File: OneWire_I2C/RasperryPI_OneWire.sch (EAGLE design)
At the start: 21 parts, among them U1 P82B715D, U2 DS2482-800

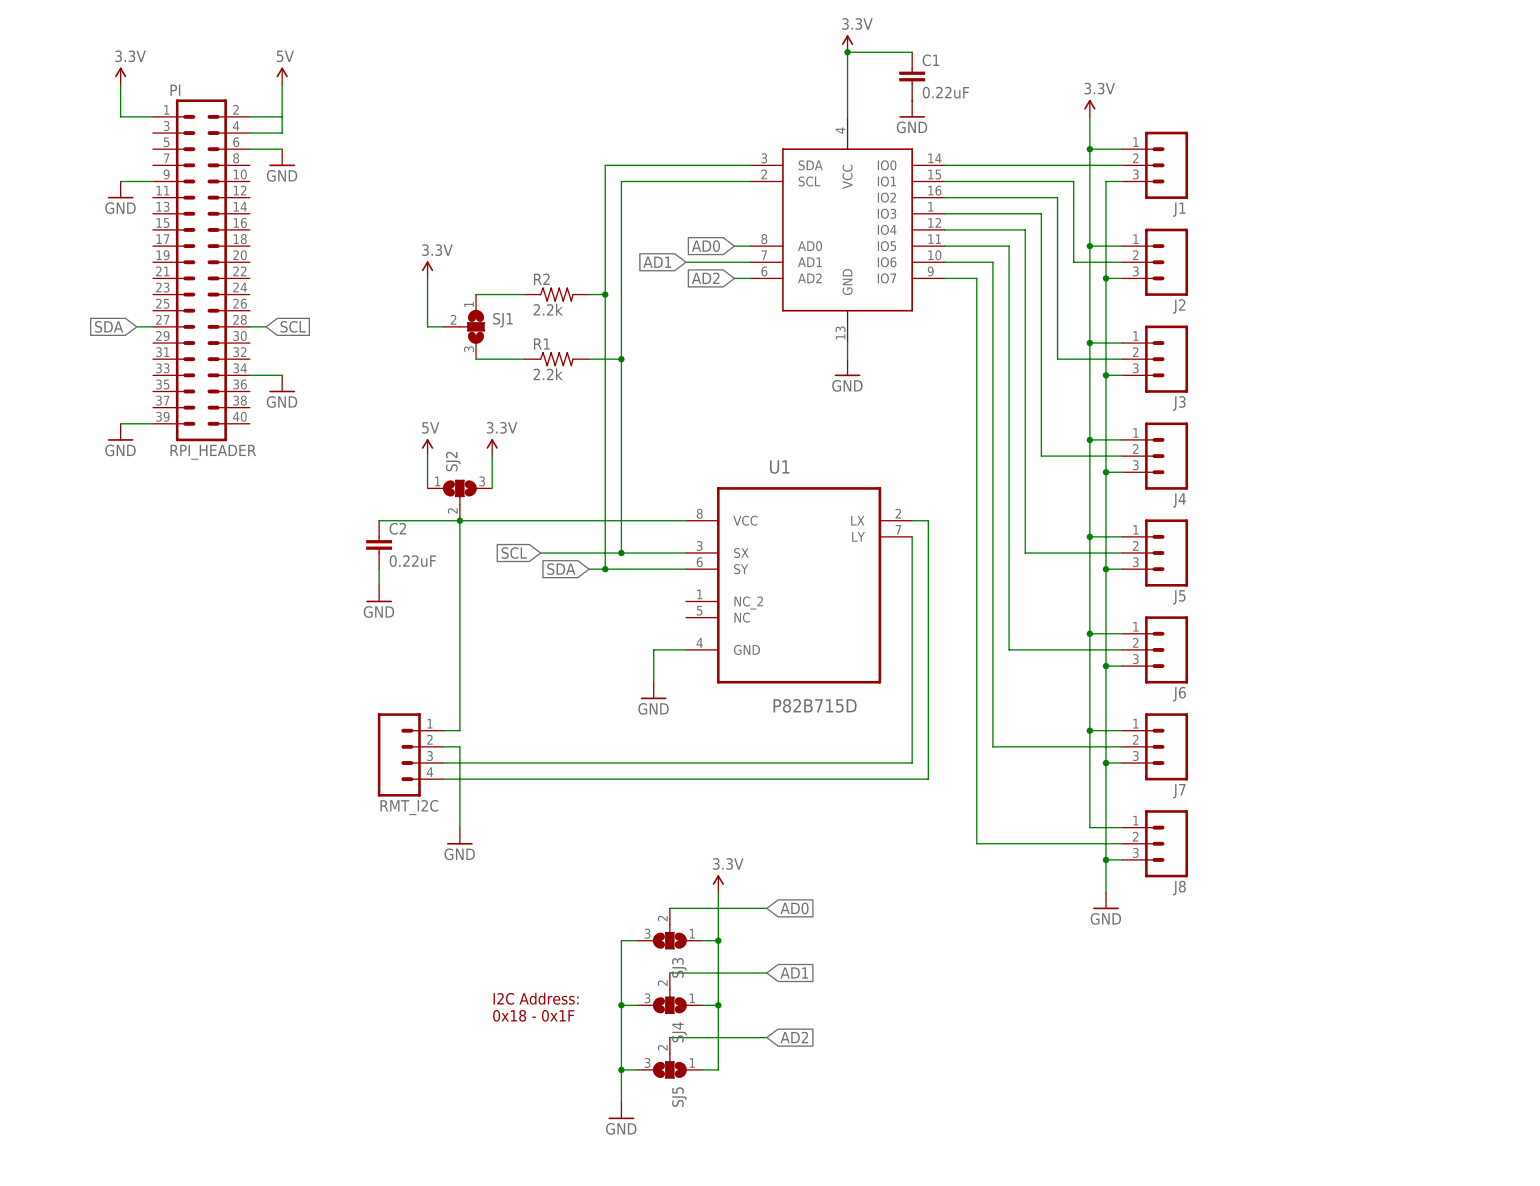
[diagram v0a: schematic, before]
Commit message: Added Raspberry pi board, updated I2C extender pullup resistors to other boards
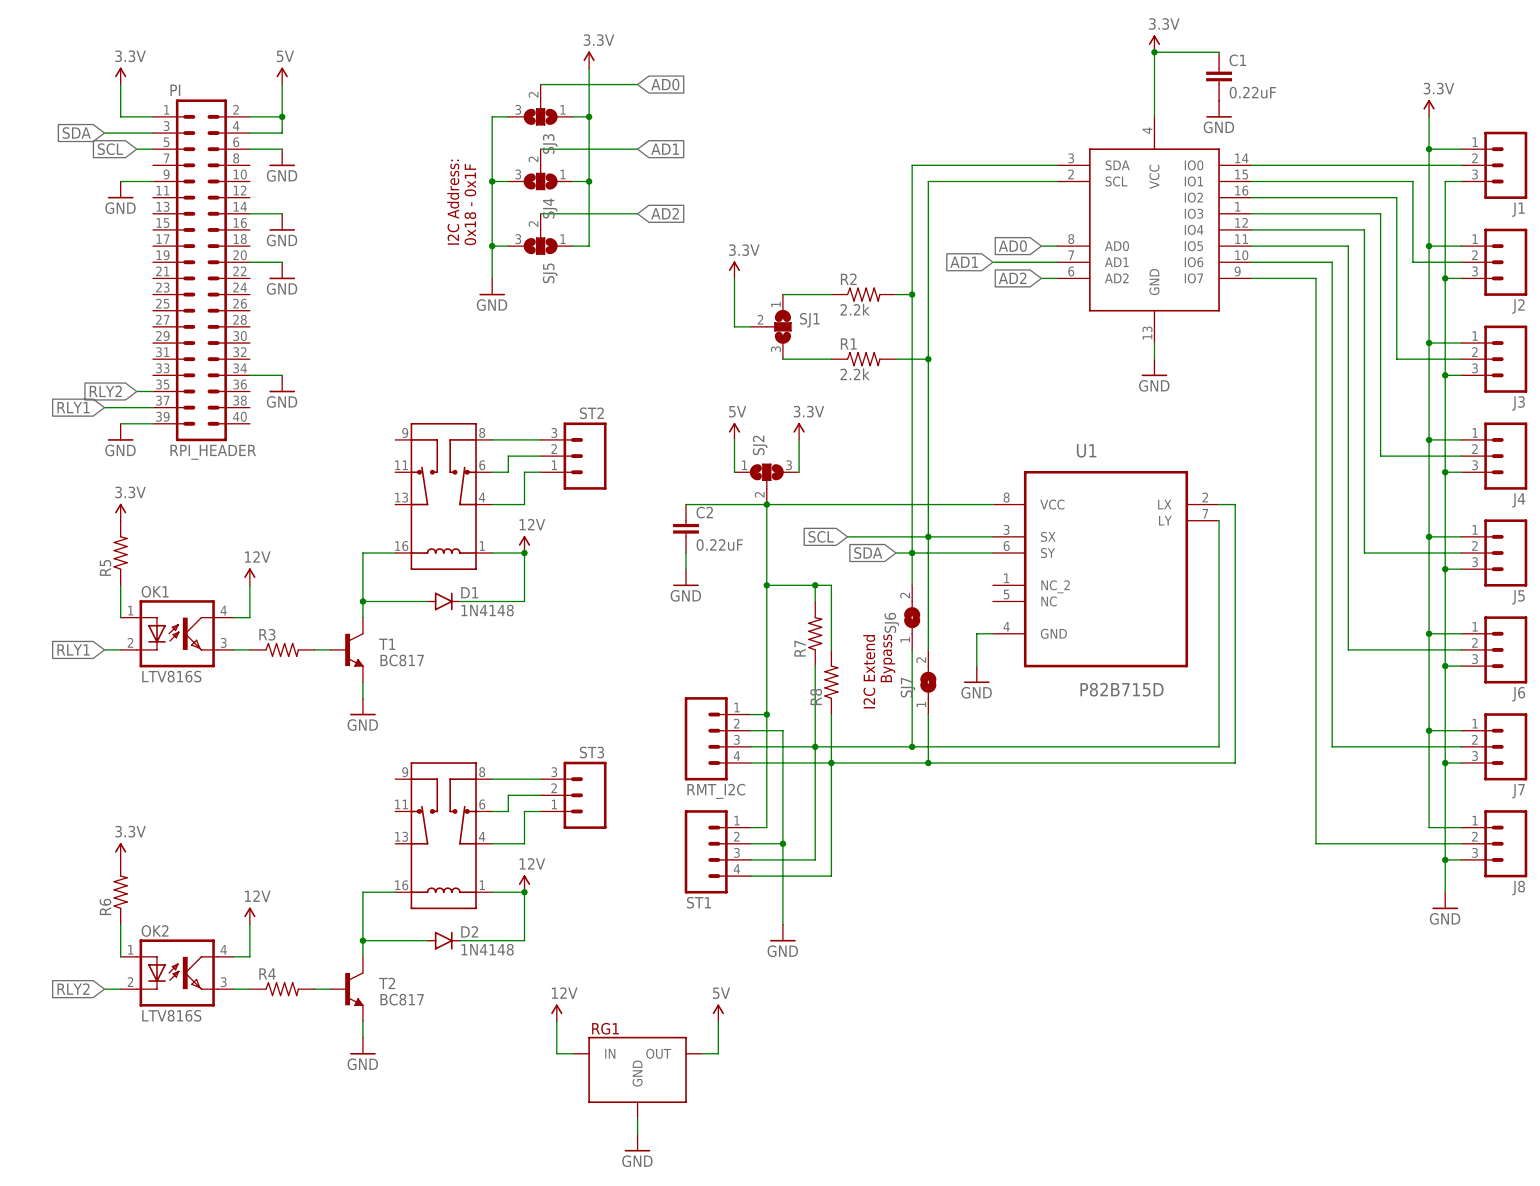
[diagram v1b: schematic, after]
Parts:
- added D1, D2: 1N4148, SparkFun-DiscreteSemi:DIODE1N4148
- added OK1, OK2: LTV816S, optocoupler:LTV816S
- added R3, R4: (no value), SparkFun-Resistors:RESISTOR0603
- added R5, R6, R7, R8: (no value), SparkFun-Resistors:RESISTOR0805-RES
- added RG1: (no value), Puffin:MURATA_REG
- added RLY1, RLY2: HK19F_5V_DPDT_RELAY, Puffin:HK19F_5V_DPDT_RELAY
- added SJ6, SJ7: (no value), jumper:SJ
- added ST1: (no value), Puffin:SCREWTERM_4
- added ST2, ST3: (no value), Puffin:SCREWTERM_3
- added T1, T2: BC817, Puffin:BC817
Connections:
- new net 12V: D1.C, D2.C, OK1.COL, OK2.COL, RG1.IN, RLY1.L1, RLY2.L1
- new net N$12: R4.2, T2.B
- new net N$13: D2.A, RLY2.L2, T2.C
- new net N$14: D1.A, RLY1.L2, T1.C
- new net N$15: R3.2, T1.B
- new net N$16: OK1.EMIT, R3.1
- new net N$17: RLY2.C1, ST3.1
- new net N$18: RLY2.NC1, ST3.2
- new net N$19: RLY2.NO1, ST3.3
- new net N$20: RLY1.C1, ST2.1
- new net N$21: RLY1.NC1, ST2.2
- new net N$22: RLY1.NO1, ST2.3
- new net N$23: OK2.A, R6.1
- new net N$24: OK1.A, R5.1
- new net RLY1: OK1.C, PI.37
- new net RLY2: OK2.C, PI.35
- new net VSEL: C2.1, R7.2, R8.2, RMT_I2C.1, SJ2.2, ST1.1, U1.VCC
- net 3.3V: now also R5.2, R6.2
- net 5V: now also RG1.OUT
- net GND: now also PI.14, PI.20, RG1.GND, ST1.2, T1.E, T2.E
- net LCL: now also R8.1, SJ7.1, ST1.4
- net LDA: now also R7.1, SJ6.1, ST1.3
- net N$11: now also OK2.EMIT, R4.1; no longer C2.1, RMT_I2C.1, SJ2.2, U1.VCC
- net SCL: now also PI.5, SJ7.2; no longer PI.28
- net SDA: now also PI.3, SJ6.2; no longer PI.27
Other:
- note added: "I2C Extend Bypass"
- moved on the sheet: C1, C2, J1, J2, J3, J4, J5, J6, J7, J8, R1, R2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

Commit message: Finished RPI 1Wire board
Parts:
- removed RMT_I2C: (no value), SparkFun-Connectors:M04PTH
- removed SJ1: (no value), jumper:SJ2W
- removed ST1: (no value), Puffin:SCREWTERM_4
- added J10, J11, J9: MOLEX_MINILITE_TRAP_2, Puffin:MOLEX_MINILITE_TRAP_2
- added R10, R9: (no value), Puffin:POT_3MM
- R1, R2: value 2.2k -> (none); device SparkFun-Resistors:2.2KOHM-1/10W-1%(0603) -> SparkFun-Resistors:RESISTOR0805-RES
- R3, R4: device SparkFun-Resistors:RESISTOR0603 -> SparkFun-Resistors:RESISTOR0805-RES
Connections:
- removed net N$8: R2.1, SJ1.1
- removed net N$9: R1.1, SJ1.3
- new net N$25: R10.2, R7.2
- new net N$26: R8.2, R9.2
- net 12V: now also J11.1, J9.1
- net 3.3V: now also J1.2, J2.2, J3.2, J4.2, J5.2, J6.2, J7.2, J8.2, R1.2, R2.2; no longer J1.1, J2.1, J3.1, J4.1, J5.1, J6.1, J7.1, J8.1, R5.2, R6.2, SJ1.2
- net GND: now also J10.2, J11.2, R5.1, R6.1; no longer RMT_I2C.2, ST1.2
- net LCL: now also J10.1; no longer RMT_I2C.4, ST1.4
- net LDA: now also J9.2; no longer RMT_I2C.3, ST1.3
- net N$1: now also J1.1; no longer J1.2
- net N$10: now also J8.1; no longer J8.2
- net N$17: now also RLY2.C2
- net N$18: now also RLY2.NC2
- net N$19: now also RLY2.NO2
- net N$2: now also J2.1; no longer J2.2
- net N$20: now also RLY1.C2
- net N$21: now also RLY1.NC2
- net N$22: now also RLY1.NO2
- net N$23: now also OK1.C, R5.2; no longer OK2.A, R6.1
- net N$24: now also OK2.C, R6.2; no longer OK1.A, R5.1
- net N$3: now also J3.1; no longer J3.2
- net N$4: now also J4.1; no longer J4.2
- net N$5: now also J5.1; no longer J5.2
- net N$6: now also J6.1; no longer J6.2
- net N$7: now also J7.1; no longer J7.2
- net RLY1: now also OK1.A; no longer OK1.C
- net RLY2: now also OK2.A; no longer OK2.C
- net SCL: now also R2.1; no longer R1.2
- net SDA: now also R1.1; no longer R2.2
- net VSEL: now also R10.1, R9.1; no longer R7.2, R8.2, RMT_I2C.1, ST1.1
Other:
- moved on the sheet: C2, D1, D2, OK1, OK2, R1, R2, R3, R4, R5, R6, R7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

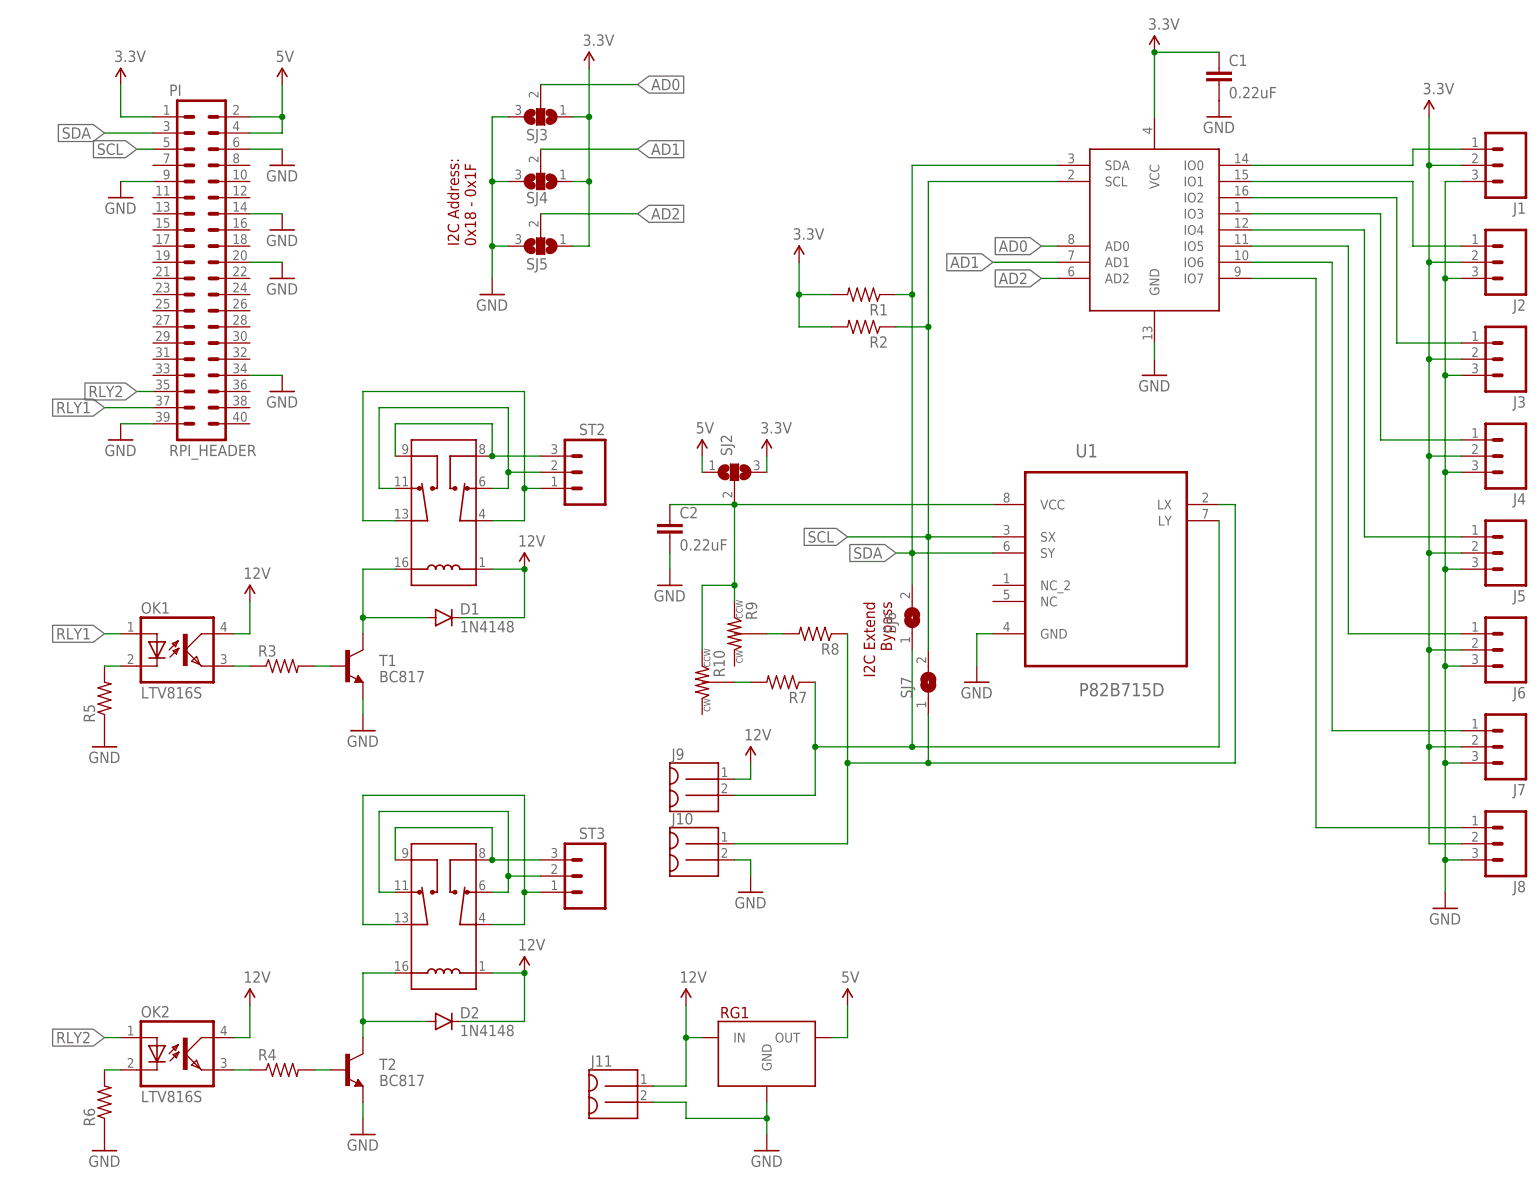
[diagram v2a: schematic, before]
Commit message: Standardized i2c connections, fixed 1Wire connections, lots of cleanup
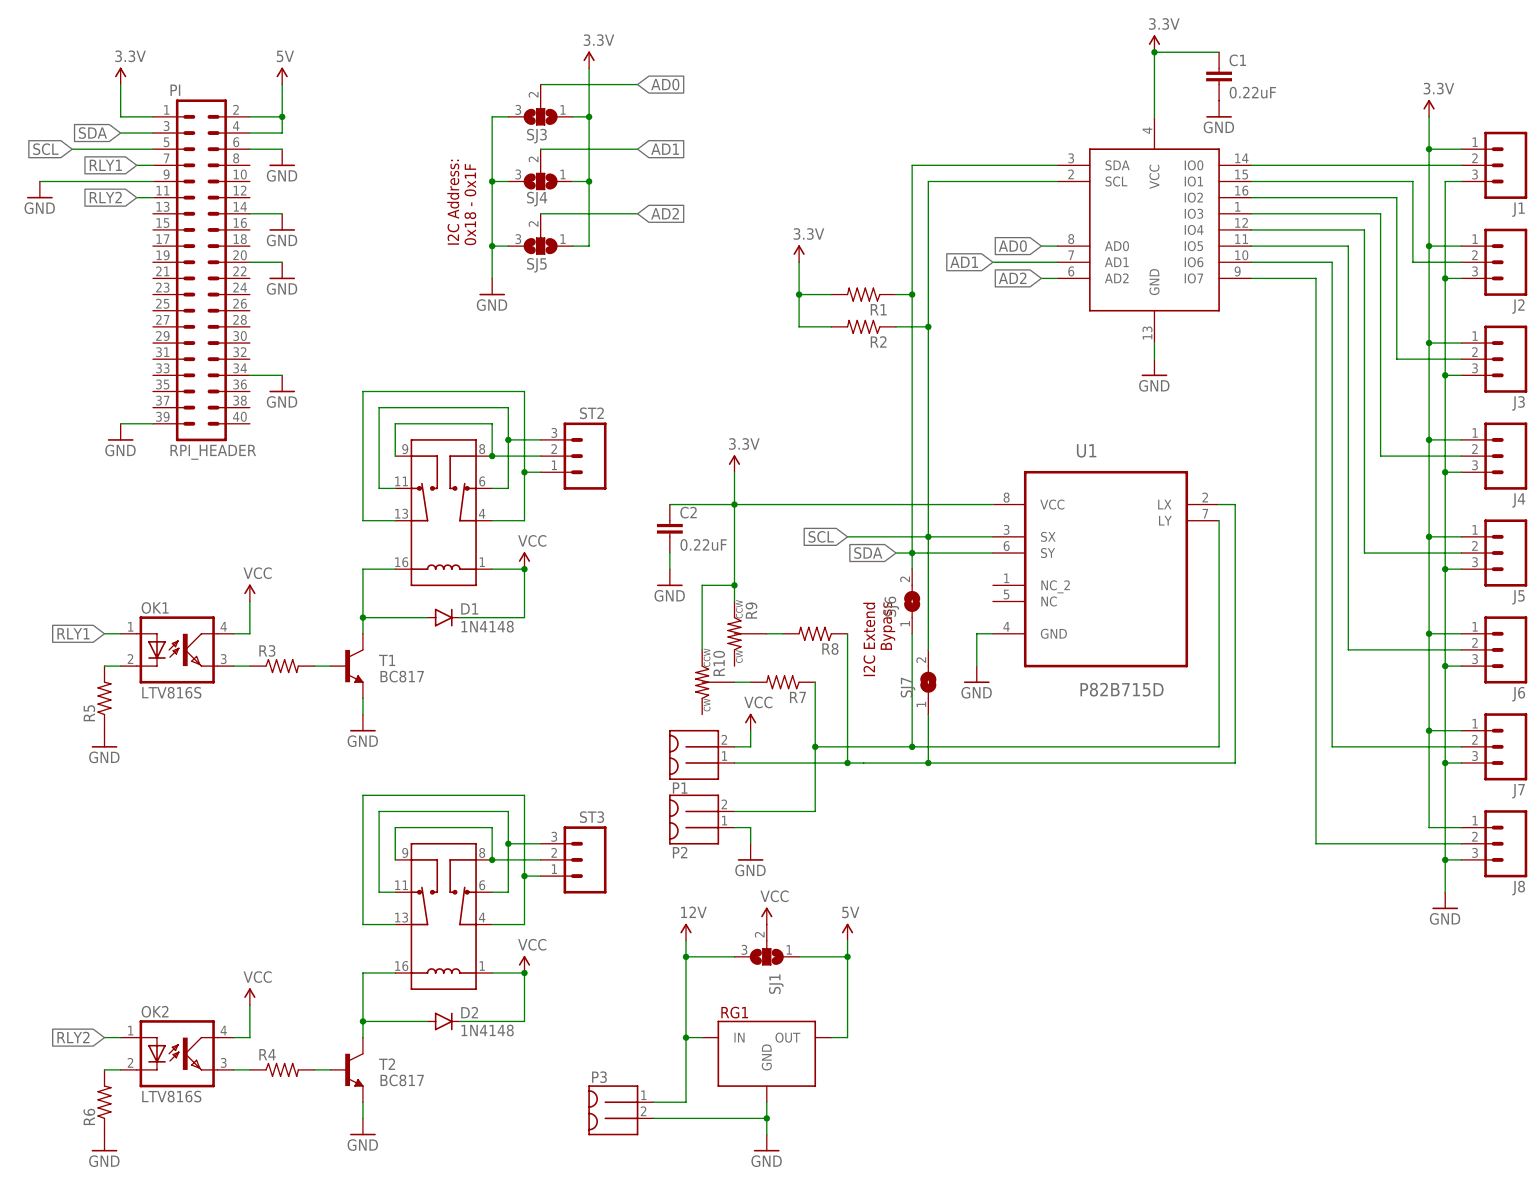
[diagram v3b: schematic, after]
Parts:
- removed J10, J11, J9: MOLEX_MINILITE_TRAP_2, Puffin:MOLEX_MINILITE_TRAP_2
- removed SJ2: (no value), jumper:SJ2W
- added P1, P2, P3: MOLEX_MINILITE_TRAP_2, Puffin:MOLEX_MINILITE_TRAP_2
- added SJ1: (no value), jumper:SJ2W
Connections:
- removed net VSEL: C2.1, R10.1, R9.1, SJ2.2, U1.VCC
- new net VCC: D1.C, D2.C, OK1.COL, OK2.COL, P1.2, RLY1.L1, RLY2.L1, SJ1.2
- net 12V: now also P3.1, SJ1.3; no longer D1.C, D2.C, J11.1, J9.1, OK1.COL, OK2.COL, RLY1.L1, RLY2.L1
- net 3.3V: now also C2.1, J1.1, J2.1, J3.1, J4.1, J5.1, J6.1, J7.1, J8.1, R10.1, R9.1, U1.VCC; no longer J1.2, J2.2, J3.2, J4.2, J5.2, J6.2, J7.2, J8.2, SJ2.3
- net 5V: now also SJ1.1; no longer SJ2.1
- net GND: now also P2.1, P3.2; no longer J10.2, J11.2
- net LCL: now also P1.1; no longer J10.1
- net LDA: now also P2.2; no longer J9.2
- net N$1: now also J1.2; no longer J1.1
- net N$10: now also J8.2; no longer J8.1
- net N$18: now also ST3.3; no longer ST3.2
- net N$19: now also ST3.2; no longer ST3.3
- net N$2: now also J2.2; no longer J2.1
- net N$21: now also ST2.3; no longer ST2.2
- net N$22: now also ST2.2; no longer ST2.3
- net N$3: now also J3.2; no longer J3.1
- net N$4: now also J4.2; no longer J4.1
- net N$5: now also J5.2; no longer J5.1
- net N$6: now also J6.2; no longer J6.1
- net N$7: now also J7.2; no longer J7.1
- net RLY1: now also PI.7; no longer PI.37
- net RLY2: now also PI.11; no longer PI.35
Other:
- moved on the sheet: SJ6, ST2, ST3

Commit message: Gate 4, and misc updates
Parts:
- renumbered ST3 to ST1
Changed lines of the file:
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@@
 <part name="RLY2" library="Puffin" deviceset="HK19F_5V_DPDT_RELAY" device=""/>
 <part name="ST2" library="Puffin" deviceset="SCREWTERM_3" device=""/>
-<part name="ST3" library="Puffin" deviceset="SCREWTERM_3" device=""/>
+<part name="ST1" library="Puffin" deviceset="SCREWTERM_3" device=""/>
 <part name="T2" library="Puffin" deviceset="BC817" device=""/>
 <part name="T1" library="Puffin" deviceset="BC817" device=""/>
@@
 <instance part="RLY2" gate="G$1" x="68.58" y="38.1" rot="R90"/>
 <instance part="ST2" gate="G$1" x="91.44" y="116.84" rot="MR0"/>
-<instance part="ST3" gate="G$1" x="91.44" y="53.34" rot="MR0"/>
+<instance part="ST1" gate="G$1" x="91.44" y="53.34" rot="MR0"/>
 <instance part="T2" gate="G$1" x="53.34" y="17.78"/>
 <instance part="T1" gate="G$1" x="53.34" y="81.28"/>
@@
 <wire x1="76.2" y1="40.64" x2="81.28" y2="40.64" width="0.1524" layer="91"/>
 <wire x1="81.28" y1="40.64" x2="81.28" y2="48.26" width="0.1524" layer="91"/>
-<pinref part="ST3" gate="G$1" pin="1"/>
+<pinref part="ST1" gate="G$1" pin="1"/>
 <wire x1="81.28" y1="48.26" x2="83.82" y2="48.26" width="0.1524" layer="91"/>
 <wire x1="81.28" y1="48.26" x2="81.28" y2="60.96" width="0.1524" layer="91"/>
@@
 <pinref part="RLY2" gate="G$1" pin="NC2"/>
 <wire x1="58.42" y1="45.72" x2="60.96" y2="45.72" width="0.1524" layer="91"/>
-<pinref part="ST3" gate="G$1" pin="3"/>
+<pinref part="ST1" gate="G$1" pin="3"/>
 <wire x1="83.82" y1="53.34" x2="78.74" y2="53.34" width="0.1524" layer="91"/>
 <junction x="78.74" y="53.34"/>
@@
 <wire x1="76.2" y1="55.88" x2="60.96" y2="55.88" width="0.1524" layer="91"/>
 <wire x1="60.96" y1="55.88" x2="60.96" y2="50.8" width="0.1524" layer="91"/>
-<pinref part="ST3" gate="G$1" pin="2"/>
+<pinref part="ST1" gate="G$1" pin="2"/>
 <wire x1="83.82" y1="50.8" x2="76.2" y2="50.8" width="0.1524" layer="91"/>
 <junction x="76.2" y="50.8"/>
